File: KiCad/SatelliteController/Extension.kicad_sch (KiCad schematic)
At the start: 3 parts, among them J7 CONN_STATUS_PANEL, J8 CONN_PANEL_BAORD_2, J9 CONN_PANEL_BAORD_1

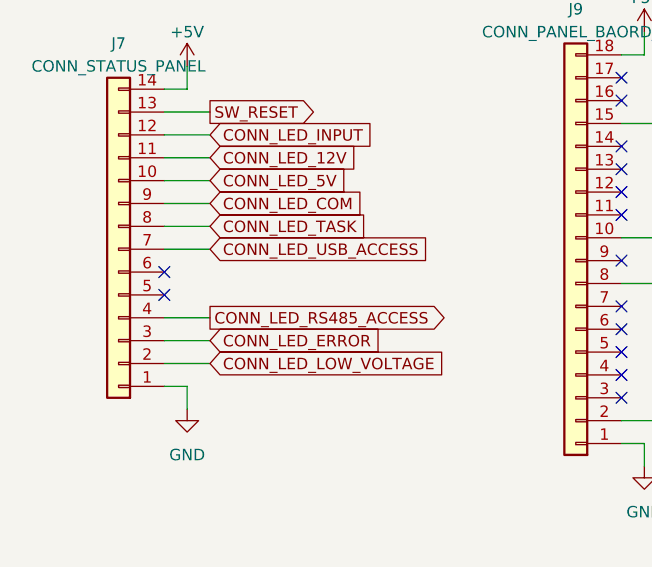
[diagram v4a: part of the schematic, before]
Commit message: 7セグ用コネクタを6Pから14Pの空いているピンに押し込んだ
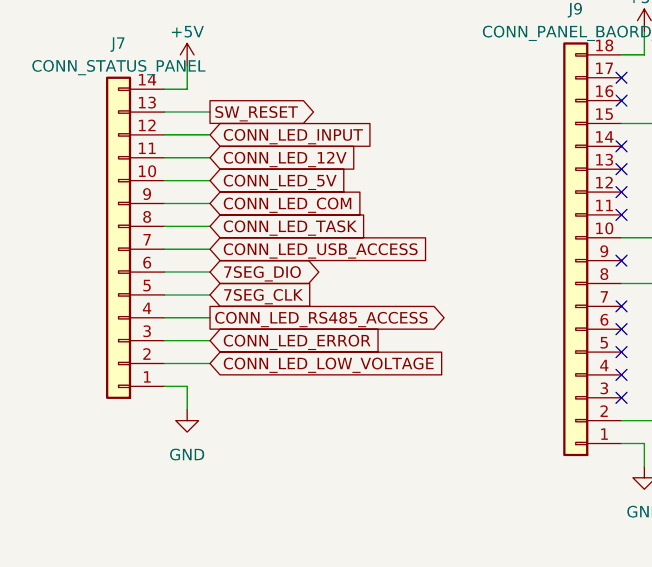
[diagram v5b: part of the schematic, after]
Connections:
- net 7SEG_CLK: now reaches J7.5 (Pin_5)
- net 7SEG_DIO: now reaches J7.6 (Pin_6)
- no-connect marks 24 -> 22
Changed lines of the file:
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@@
   (paper "A4")
   (no_connect (at 83.82 49.53))
-  (no_connect (at 33.02 63.5))
   (no_connect (at 83.82 52.07))
   (no_connect (at 83.82 77.47))
@@
   (no_connect (at 125.73 63.5))
   (no_connect (at 83.82 57.15))
-  (no_connect (at 33.02 66.04))
   (no_connect (at 83.82 41.91))
   (wire (pts (xy 86.36 36.83) (xy 86.36 39.37))
@@
     (stroke (width 0) (type default))
   )
+  (wire (pts (xy 33.02 63.5) (xy 38.1 63.5))
+    (stroke (width 0) (type default))
+  )
   (wire (pts (xy 33.02 60.96) (xy 38.1 60.96))
     (stroke (width 0) (type default))
@@
     (stroke (width 0) (type default))
   )
+  (wire (pts (xy 33.02 66.04) (xy 38.1 66.04))
+    (stroke (width 0) (type default))
+  )
   (wire (pts (xy 125.73 58.42) (xy 128.27 58.42))
     (stroke (width 0) (type default))
@@
     )
   )
+  (global_label "7SEG_CLK" (shape input) (at 38.1 66.04 0) (fields_autoplaced)
+    (effects (font (size 1.27 1.27)) (justify left))
+    (property "Intersheetrefs" "${INTERSHEET_REFS}" (at 50.3795 66.04 0)
+      (effects (font (size 1.27 1.27)) (justify left) hide)
+    )
+  )
   (global_label "CONN_LED_OPEN" (shape output) (at 128.27 53.34 0) (fields_autoplaced)
     (effects (font (size 1.27 1.27)) (justify left))
@@
       (effects (font (size 1.27 1.27)) (justify left) hide)
     )
+  )
+  (global_label "7SEG_DIO" (shape bidirectional) (at 38.1 63.5 0) (fields_autoplaced)
+    (effects (font (size 1.27 1.27)) (justify left))
+    (property "Intersheetrefs" "${INTERSHEET_REFS}" (at 51.128 63.5 0)
+      (effects (font (size 1.27 1.27)) (justify left) hide)
+    )

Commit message: コネクタをまとめた
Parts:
- removed J9: CONN_PANEL_BAORD_1, TSRP_Connector_Hirose:DF51A-18DP-2DS, symbol Connector_Generic:Conn_01x18
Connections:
- net SW_KILL: now also J8.8 (Pin_8)
- net SW_PURGE: now also J8.21 (Pin_21)
- net SW_RUN: now also J8.10 (Pin_10)
- net SW_SAFETY: now also J8.19 (Pin_19)
- no-connect marks 22 -> 6
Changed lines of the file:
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@@
 (kicad_sch (version 20230121) (generator eeschema)
   (paper "A4")
-  (no_connect (at 83.82 49.53))
-  (no_connect (at 83.82 52.07))
-  (no_connect (at 83.82 77.47))
   (no_connect (at 125.73 66.04))
-  (no_connect (at 125.73 40.64))
-  (no_connect (at 83.82 74.93))
-  (no_connect (at 83.82 54.61))
-  (no_connect (at 83.82 67.31))
-  (no_connect (at 125.73 35.56))
-  (no_connect (at 83.82 62.23))
-  (no_connect (at 83.82 44.45))
-  (no_connect (at 125.73 68.58))
   (no_connect (at 125.73 78.74))
-  (no_connect (at 83.82 72.39))
   (no_connect (at 125.73 71.12))
   (no_connect (at 125.73 81.28))
   (no_connect (at 125.73 76.2))
-  (no_connect (at 83.82 69.85))
   (no_connect (at 125.73 73.66))
-  (no_connect (at 125.73 63.5))
-  (no_connect (at 83.82 57.15))
-  (no_connect (at 83.82 41.91))
-  (wire (pts (xy 86.36 36.83) (xy 86.36 39.37))
-    (stroke (width 0) (type default))
-  )
   (wire (pts (xy 125.73 45.72) (xy 128.27 45.72))
     (stroke (width 0) (type default))
@@
     (stroke (width 0) (type default))
   )
+  (wire (pts (xy 125.73 63.5) (xy 128.27 63.5))
+    (stroke (width 0) (type default))
+  )
   (wire (pts (xy 33.02 63.5) (xy 38.1 63.5))
     (stroke (width 0) (type default))
@@
     (stroke (width 0) (type default))
   )
-  (wire (pts (xy 83.82 64.77) (xy 88.9 64.77))
-    (stroke (width 0) (type default))
-  )
   (wire (pts (xy 33.02 53.34) (xy 38.1 53.34))
     (stroke (width 0) (type default))
@@
     (stroke (width 0) (type default))
   )
-  (wire (pts (xy 83.82 80.01) (xy 88.9 80.01))
-    (stroke (width 0) (type default))
-  )
-  (wire (pts (xy 83.82 46.99) (xy 88.9 46.99))
+  (wire (pts (xy 125.73 40.64) (xy 128.27 40.64))
     (stroke (width 0) (type default))
   )
@@
     (stroke (width 0) (type default))
   )
-  (wire (pts (xy 83.82 59.69) (xy 88.9 59.69))
-    (stroke (width 0) (type default))
-  )
   (wire (pts (xy 125.73 83.82) (xy 128.27 83.82))
     (stroke (width 0) (type default))
   )
-  (wire (pts (xy 86.36 39.37) (xy 83.82 39.37))
-    (stroke (width 0) (type default))
-  )
   (wire (pts (xy 35.56 76.2) (xy 35.56 78.74))
     (stroke (width 0) (type default))
   )
-  (wire (pts (xy 86.36 82.55) (xy 86.36 85.09))
-    (stroke (width 0) (type default))
-  )
-  (wire (pts (xy 83.82 82.55) (xy 86.36 82.55))
+  (wire (pts (xy 125.73 68.58) (xy 128.27 68.58))
+    (stroke (width 0) (type default))
+  )
+  (wire (pts (xy 125.73 35.56) (xy 128.27 35.56))
     (stroke (width 0) (type default))
   )
@@
     )
   )
-  (global_label "SW_KILL" (shape output) (at 88.9 64.77 0) (fields_autoplaced)
-    (effects (font (size 1.27 1.27)) (justify left))
-    (property "Intersheetrefs" "${INTERSHEET_REFS}" (at 99.3653 64.77 0)
+  (global_label "SW_KILL" (shape output) (at 128.27 68.58 0) (fields_autoplaced)
+    (effects (font (size 1.27 1.27)) (justify left))
+    (property "Intersheetrefs" "${INTERSHEET_REFS}" (at 138.7353 68.58 0)
       (effects (font (size 1.27 1.27)) (justify left) hide)
     )
@@
     )
   )
-  (global_label "SW_PURGE" (shape output) (at 88.9 46.99 0) (fields_autoplaced)
-    (effects (font (size 1.27 1.27)) (justify left))
-    (property "Intersheetrefs" "${INTERSHEET_REFS}" (at 101.7238 46.99 0)
+  (global_label "SW_PURGE" (shape output) (at 128.27 35.56 0) (fields_autoplaced)
+    (effects (font (size 1.27 1.27)) (justify left))
+    (property "Intersheetrefs" "${INTERSHEET_REFS}" (at 141.0938 35.56 0)
       (effects (font (size 1.27 1.27)) (justify left) hide)
     )
@@
     )
   )
-  (global_label "SW_RUN" (shape output) (at 88.9 59.69 0) (fields_autoplaced)
-    (effects (font (size 1.27 1.27)) (justify left))
-    (property "Intersheetrefs" "${INTERSHEET_REFS}" (at 99.3653 59.69 0)
-      (effects (font (size 1.27 1.27)) (justify left) hide)
-    )
-  )
-  (global_label "SW_SAFETY" (shape output) (at 88.9 80.01 0) (fields_autoplaced)
-    (effects (font (size 1.27 1.27)) (justify left))
-    (property "Intersheetrefs" "${INTERSHEET_REFS}" (at 102.0262 80.01 0)
+  (global_label "SW_RUN" (shape output) (at 128.27 63.5 0) (fields_autoplaced)
+    (effects (font (size 1.27 1.27)) (justify left))
+    (property "Intersheetrefs" "${INTERSHEET_REFS}" (at 138.7353 63.5 0)
+      (effects (font (size 1.27 1.27)) (justify left) hide)
+    )
+  )
+  (global_label "SW_SAFETY" (shape output) (at 128.27 40.64 0) (fields_autoplaced)
+    (effects (font (size 1.27 1.27)) (justify left))
+    (property "Intersheetrefs" "${INTERSHEET_REFS}" (at 141.3962 40.64 0)
       (effects (font (size 1.27 1.27)) (justify left) hide)
     )
@@
     )
   )
-  (symbol (lib_id "Connector_Generic:Conn_01x18") (at 78.74 62.23 180) (unit 1)
-    (in_bom yes) (on_board yes) (dnp no) (fields_autoplaced)
-    (property "Reference" "J9" (at 78.74 34.29 0)
-      (effects (font (size 1.27 1.27)))
-    )
-    (property "Value" "CONN_PANEL_BAORD_1" (at 78.74 36.83 0)
-      (effects (font (size 1.27 1.27)))
-    )
-    (property "Footprint" "TSRP_Connector_Hirose:DF51A-18DP-2DS" (at 78.74 62.23 0)
-      (effects (font (size 1.27 1.27)) hide)
-    )
-    (property "Datasheet" "~" (at 78.74 62.23 0)
-      (effects (font (size 1.27 1.27)) hide)
-    )
-    (property "LCSC" "" (at 78.74 62.23 0)
-      (effects (font (size 1.27 1.27)) hide)
-    )
-    (pin "1")
-    (pin "10")
-    (pin "11")
-    (pin "12")
-    (pin "13")
-    (pin "14")
-    (pin "15")
-    (pin "16")
-    (pin "17")
-    (pin "18")
-    (pin "2")
-    (pin "3")
-    (pin "4")
-    (pin "5")
-    (pin "6")
-    (pin "7")
-    (pin "8")
-    (pin "9")
-    (instances
-      (project "SatelliteController"
-        (path "/628d040b-43bf-4733-804f-091644a90124/7294b7f8-79a7-4ea3-8687-92a673d94882"
-          (reference "J9") (unit 1)
-        )
-      )
-    )
-  )
-  (symbol (lib_id "power:+5V") (at 86.36 36.83 0) (unit 1)
-    (in_bom yes) (on_board yes) (dnp no) (fields_autoplaced)
-    (property "Reference" "#PWR046" (at 86.36 40.64 0)
-      (effects (font (size 1.27 1.27)) hide)
-    )
-    (property "Value" "+5V" (at 86.36 33.02 0)
-      (effects (font (size 1.27 1.27)))
-    )
-    (property "Footprint" "" (at 86.36 36.83 0)
-      (effects (font (size 1.27 1.27)) hide)
-    )
-    (property "Datasheet" "" (at 86.36 36.83 0)
-      (effects (font (size 1.27 1.27)) hide)
-    )
-    (pin "1")
-    (instances
-      (project "SatelliteController"
-        (path "/628d040b-43bf-4733-804f-091644a90124"
-          (reference "#PWR046") (unit 1)
-        )
-        (path "/628d040b-43bf-4733-804f-091644a90124/7294b7f8-79a7-4ea3-8687-92a673d94882"
-          (reference "#PWR049") (unit 1)
-        )
-      )
-    )
-  )
   (symbol (lib_id "power:+5V") (at 128.27 30.48 0) (unit 1)
     (in_bom yes) (on_board yes) (dnp no) (fields_autoplaced)
@@
         )
       )
-    )
-  )
-  (symbol (lib_id "power:GND") (at 86.36 85.09 0) (unit 1)
-    (in_bom yes) (on_board yes) (dnp no) (fields_autoplaced)
-    (property "Reference" "#PWR052" (at 86.36 91.44 0)
-      (effects (font (size 1.27 1.27)) hide)
-    )
-    (property "Value" "GND" (at 86.36 90.17 0)
-      (effects (font (size 1.27 1.27)))
-    )
-    (property "Footprint" "" (at 86.36 85.09 0)
-      (effects (font (size 1.27 1.27)) hide)
-    )
-    (property "Datasheet" "" (at 86.36 85.09 0)
-      (effects (font (size 1.27 1.27)) hide)
-    )
-    (pin "1")
-    (instances
-      (project "SatelliteController"
-        (path "/628d040b-43bf-4733-804f-091644a90124/7294b7f8-79a7-4ea3-8687-92a673d94882"
-          (reference "#PWR052") (unit 1)
-        )
-      )
